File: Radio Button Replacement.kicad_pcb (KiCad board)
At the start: 2 copper layers, 40 x 40 mm, 19 parts, among them SW1 SW_Push_SPDT_1_3_2, SW2 SW_Push_SPDT_1_3_2, SW3 SW_Push_SPDT_1_3_2, SW4 SW_Push_SPDT_1_3_2

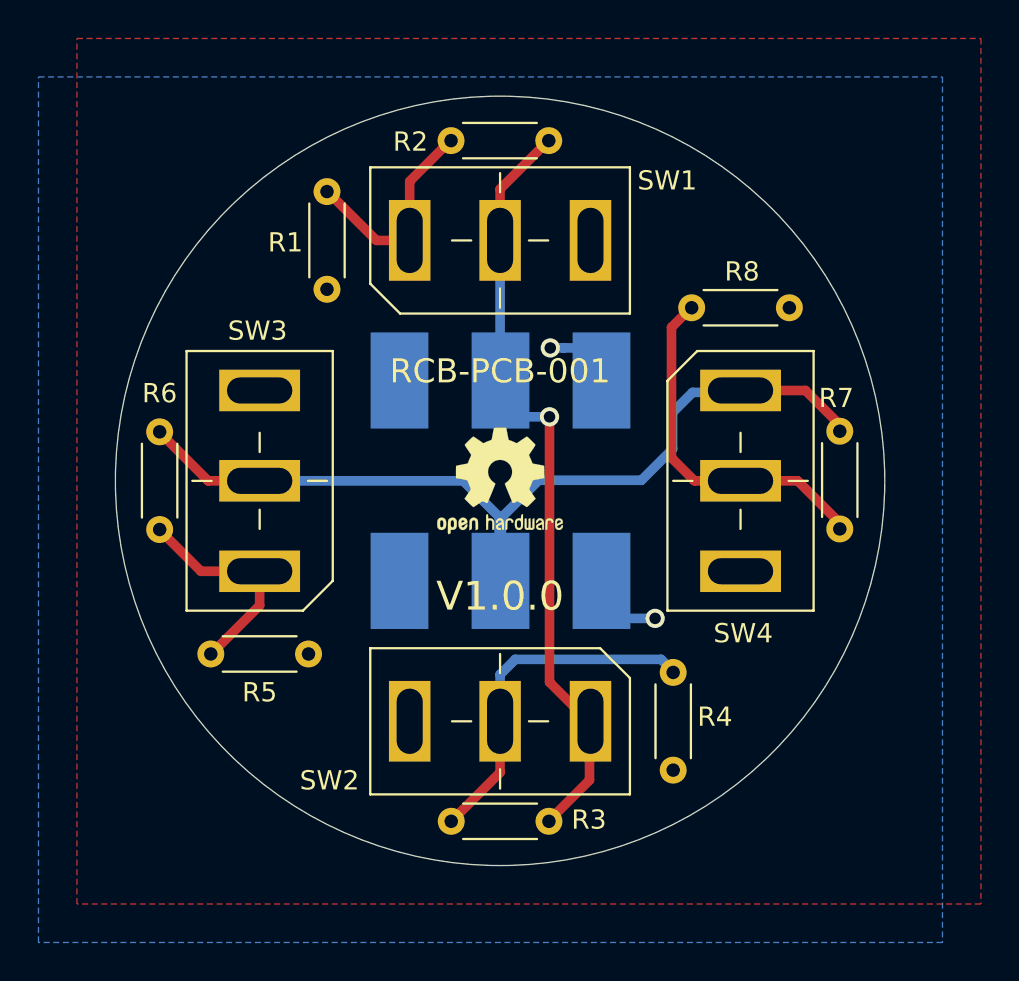
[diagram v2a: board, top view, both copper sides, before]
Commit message: Update resistor sizes
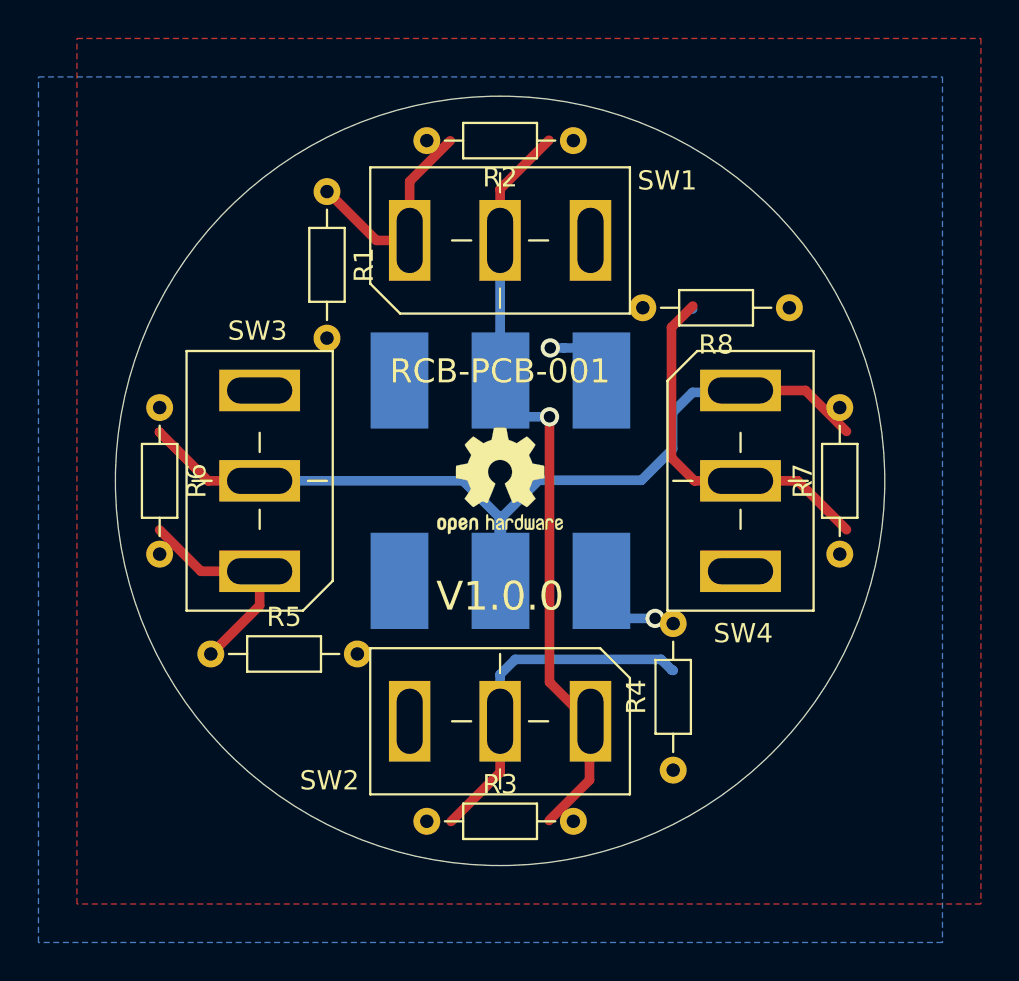
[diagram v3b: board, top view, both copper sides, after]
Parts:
- R1, R2, R3, R4, R5, R6, R7, R8: footprint Resistor_THT:R_Axial_DIN0204_L3.6mm_D1.6mm_P5.08mm_Horizontal -> Resistor_THT:R_Axial_DIN0204_L3.6mm_D1.6mm_P7.62mm_Horizontal
- moved R7 1.31 mm to (167.7, 103.8)
- moved R2 1.28 mm to (153.8, 82.3)
- moved R3 1.27 mm to (146.2, 117.7)
- moved R6 1.26 mm to (132.3, 96.2)

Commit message: Renumbering of components, PCB updates
Renumbering of components, PCB updates
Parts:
- removed the R8 at (165.0, 91.0)
- added R4: 2.2k, Resistor_THT:R_Axial_DIN0204_L3.6mm_D1.6mm_P7.62mm_Horizontal, F.Cu at (165.6, 91.0)
- moved SW1 17.7 mm to (137.5, 100.0), turned to 180 degrees
- moved SW3 17.7 mm to (150.0, 87.5), turned to 90 degrees
- moved R2 0.66 mm to (134.3, 109.0)
- moved R6 0.55 mm to (141.0, 84.4)
- moved R8 0.54 mm to (159.0, 115.6)
- renumbered R6 to R1, R5 to R2, R7 to R3, R2 to R5, R1 to R6, R3 to R7, R4 to R8, SW4 to SW2, SW2 to SW4
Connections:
- R1 pad 1: /WIRE2 -> /XWIRE
- R1 pad 2: Net-(R5-Pad1) -> Net-(R1-Pad2)
- R2 pad 1: Net-(R5-Pad1) -> Net-(R1-Pad2)
- R3 pad 2: /WIRE2 -> /XWIRE
- R5 pad 1: /WIRE1 -> /YWIRE
- R5 pad 2: Net-(R1-Pad1) -> Net-(R5-Pad2)
- R6 pad 1: Net-(R1-Pad1) -> Net-(R5-Pad2)
- R7 pad 2: /WIRE1 -> /YWIRE
- SW1 pad 1: Net-(R1-Pad1) -> Net-(R1-Pad2)
- SW1 pad 2: /WIRE1 -> /XWIRE
- SW2 pad 1: /WIRE2 -> /XWIRE
- SW3 pad 1: Net-(R5-Pad1) -> Net-(R5-Pad2)
- SW3 pad 2: /WIRE2 -> /YWIRE
- SW4 pad 1: /WIRE1 -> /YWIRE
- TP1 pad 2: /WIRE1 -> /XWIRE
- TP2 pad 2: /WIRE2 -> /YWIRE
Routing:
- net /WIRE2: track 50.2 -> 0.00 mm
- net /XWIRE: track 0.00 -> 47.9 mm
- net /YWIRE: track 0.00 -> 42.9 mm, vias 0 -> 2
- net /WIRE1: track 41.1 -> 0.00 mm, vias 1 -> 0
- net Net-(R1-Pad2): track 0.00 -> 12.1 mm
- net Net-(R5-Pad2): track 0.00 -> 11.9 mm
- net Net-(R1-Pad1): track 11.5 -> 0.00 mm
- net Net-(R5-Pad1): track 11.4 -> 0.00 mm
- net VBUS: track 7.94 -> 5.50 mm
- net Net-(R7-Pad1): track 18.3 -> 20.1 mm
- net Net-(R3-Pad1): track 19.1 -> 20.0 mm
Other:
- board text added: "X"
- board text added: "Y"
- board text removed: "1"
- board text removed: "2"

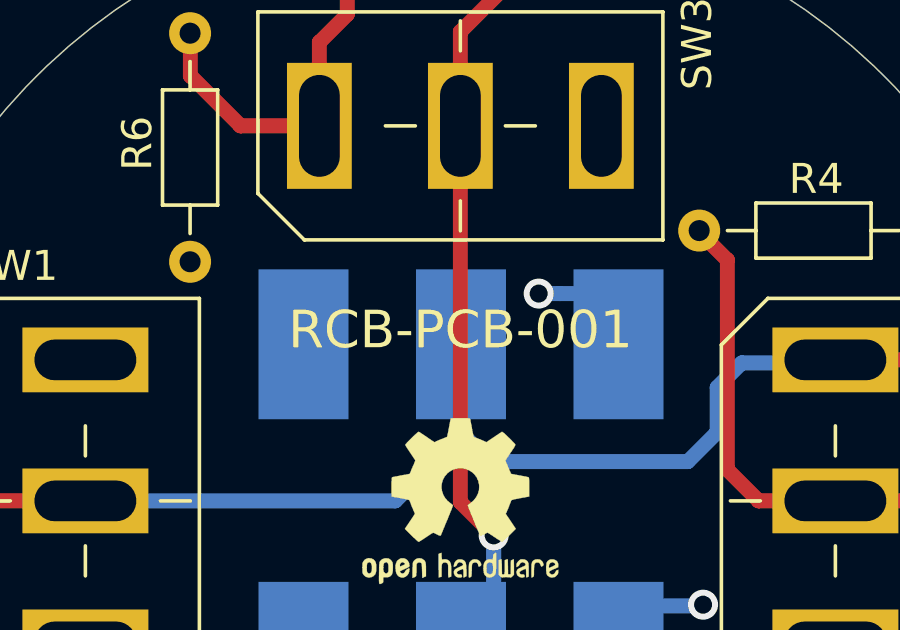
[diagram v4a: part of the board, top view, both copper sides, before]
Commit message: Update Radio Button Replacement.kicad_pcb
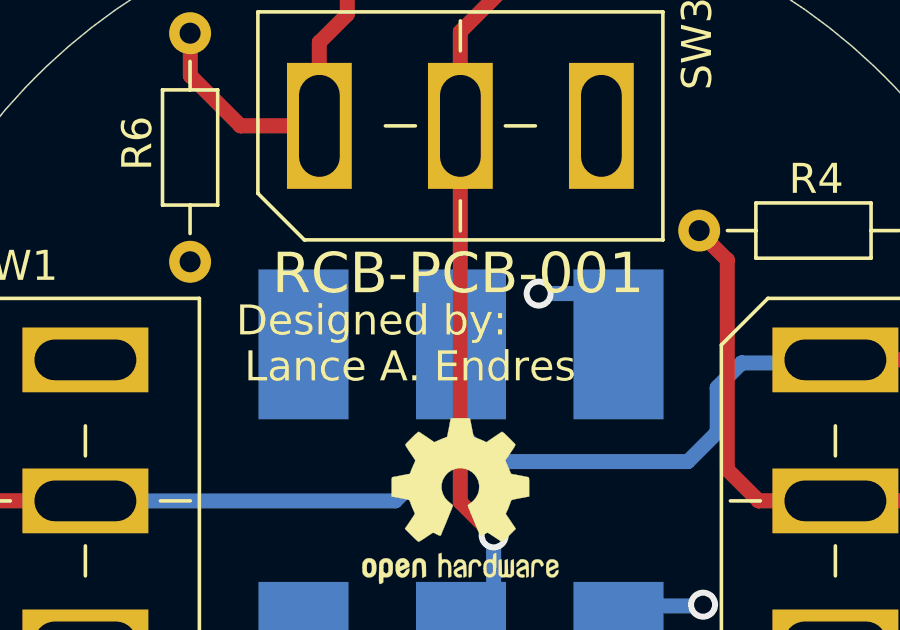
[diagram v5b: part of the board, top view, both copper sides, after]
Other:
- board text added: "Designed by:"
- board text added: "Lance A. Endres"
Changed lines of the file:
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@@
   (general
     (thickness 1.6)
-    (drawings 6)
+    (drawings 8)
     (tracks 74)
     (zones 0)
     (modules 19)
-    (nets 10)
+    (nets 9)
   )
   (page A4)
@@
   (net 5 /YWIRE)
   (net 6 /XWIRE)
-  (net 7 "Net-(SW4-Pad3)")
-  (net 8 "Net-(R1-Pad2)")
-  (net 9 "Net-(R5-Pad2)")
+  (net 7 "Net-(R1-Pad2)")
+  (net 8 "Net-(R5-Pad2)")
   (net_class Default "This is the default net class."
     (clearance 0.25)
@@
     (add_net "Net-(R5-Pad2)")
     (add_net "Net-(R7-Pad1)")
-    (add_net "Net-(SW1-Pad3)")
-    (add_net "Net-(SW2-Pad3)")
-    (add_net "Net-(SW3-Pad3)")
-    (add_net "Net-(SW4-Pad3)")
     (add_net VBUS)
   )
@@
       (net 6 /XWIRE))
     (pad 2 thru_hole oval (at 7.62 0 270) (size 1.4 1.4) (drill 0.7) (layers *.Cu *.Mask)
-      (net 8 "Net-(R1-Pad2)"))
+      (net 7 "Net-(R1-Pad2)"))
     (model ${KISYS3DMOD}/Resistor_THT.3dshapes/R_Axial_DIN0204_L3.6mm_D1.6mm_P7.62mm_Horizontal.wrl
       (at (xyz 0 0 0))
@@
       (net 1 VBUS))
     (pad 1 thru_hole circle (at 0 0) (size 1.4 1.4) (drill 0.7) (layers *.Cu *.Mask)
-      (net 8 "Net-(R1-Pad2)"))
+      (net 7 "Net-(R1-Pad2)"))
     (model ${KISYS3DMOD}/Resistor_THT.3dshapes/R_Axial_DIN0204_L3.6mm_D1.6mm_P7.62mm_Horizontal.wrl
       (at (xyz 0 0 0))
@@
       (net 5 /YWIRE))
     (pad 2 thru_hole oval (at 7.62 0 180) (size 1.4 1.4) (drill 0.7) (layers *.Cu *.Mask)
-      (net 9 "Net-(R5-Pad2)"))
+      (net 8 "Net-(R5-Pad2)"))
     (model ${KISYS3DMOD}/Resistor_THT.3dshapes/R_Axial_DIN0204_L3.6mm_D1.6mm_P7.62mm_Horizontal.wrl
       (at (xyz 0 0 0))
@@
       (net 1 VBUS))
     (pad 1 thru_hole circle (at 0 0 270) (size 1.4 1.4) (drill 0.7) (layers *.Cu *.Mask)
-      (net 9 "Net-(R5-Pad2)"))
+      (net 8 "Net-(R5-Pad2)"))
     (model ${KISYS3DMOD}/Resistor_THT.3dshapes/R_Axial_DIN0204_L3.6mm_D1.6mm_P7.62mm_Horizontal.wrl
       (at (xyz 0 0 0))
@@
       (net 5 /YWIRE))
     (pad 1 thru_hole rect (at 0 -4.7 90) (size 4.2 2.16) (drill oval 3.4 1.36) (layers *.Cu *.Mask)
-      (net 9 "Net-(R5-Pad2)"))
+      (net 8 "Net-(R5-Pad2)"))
     (model ${LE3DMOD}/8125SHZBE.step
       (offset (xyz 0 0 10))
@@
       (net 6 /XWIRE))
     (pad 1 thru_hole rect (at 0 -4.7 180) (size 4.2 2.16) (drill oval 3.4 1.36) (layers *.Cu *.Mask)
-      (net 8 "Net-(R1-Pad2)"))
+      (net 7 "Net-(R1-Pad2)"))
     (model ${LE3DMOD}/8125SHZBE.step
       (offset (xyz 0 0 10))
@@
       (net 3 GND) (solder_mask_margin 0.1016) (thermal_width 1.5))
   )
+  (gr_text "Lance A. Endres" (at 148.325238 95.52) (layer F.SilkS)
+    (effects (font (size 1 1) (thickness 0.15)))
+  )
+  (gr_text "Designed by:" (at 147.039524 93.98775) (layer F.SilkS)
+    (effects (font (size 1 1) (thickness 0.15)))
+  )
   (gr_circle (center 150 100) (end 168.05 100) (layer Dwgs.User) (width 0.05))
   (gr_text V1.0.0 (at 150 106) (layer F.SilkS)
     (effects (font (size 1.5 1.5) (thickness 0.3)))
   )
-  (gr_text RCB-PCB-001 (at 150 94.3) (layer F.SilkS)
-    (effects (font (size 1.25 1.25) (thickness 0.25)))
+  (gr_text RCB-PCB-001 (at 149.93 92.42) (layer F.SilkS)
+    (effects (font (size 1.35 1.35) (thickness 0.25)))
   )
   (gr_text Y (at 158.52 105.08) (layer B.SilkS)
@@
   )
   (gr_circle (center 150 100) (end 170 100) (layer Edge.Cuts) (width 0.05))
-  (segment (start 145.44 112.6) (end 145.46 112.58) (width 0.5) (layer B.Cu) (net 7))
   (via (at 152.61 93.09) (size 1) (drill 0.6) (layers F.Cu B.Cu) (net 1))
   (segment (start 153.317106 93.09) (end 152.61 93.09) (width 0.5) (layer B.Cu) (net 1))
@@
   (segment (start 155.34 105.24) (end 155.34 104.74) (width 0.5) (layer B.Cu) (net 1))
   (segment (start 155.34 104.74) (end 156.58 103.5) (width 0.5) (layer B.Cu) (net 1))
-  (segment (start 146.23 83.78) (end 146.23 82.32) (width 0.5) (layer F.Cu) (net 9))
-  (segment (start 145.3 87.5) (end 145.3 84.71) (width 0.5) (layer F.Cu) (net 9))
-  (segment (start 145.3 84.71) (end 146.23 83.78) (width 0.5) (layer F.Cu) (net 9))
+  (segment (start 158.9 98.96) (end 158.9 91.97) (width 0.5) (layer F.Cu) (net 2))
+  (segment (start 162.5 100) (end 159.94 100) (width 0.5) (layer F.Cu) (net 2))
+  (segment (start 158.9 91.97) (end 157.94 91.01) (width 0.5) (layer F.Cu) (net 2))
+  (segment (start 159.94 100) (end 158.9 98.96) (width 0.5) (layer F.Cu) (net 2))
+  (segment (start 162.5 100) (end 165.46 100) (width 0.5) (layer F.Cu) (net 2))
+  (segment (start 167.66 102.2) (end 167.66 103.79) (width 0.5) (layer F.Cu) (net 2))
+  (segment (start 165.46 100) (end 167.66 102.2) (width 0.5) (layer F.Cu) (net 2))
+  (segment (start 157.96 109.03) (end 158.99 108) (width 0.5) (layer B.Cu) (net 4))
+  (segment (start 151.04 109.03) (end 157.96 109.03) (width 0.5) (layer B.Cu) (net 4))
+  (segment (start 150 112.5) (end 150 110.07) (width 0.5) (layer B.Cu) (net 4))
+  (segment (start 150 110.07) (end 151.04 109.03) (width 0.5) (layer B.Cu) (net 4))
+  (segment (start 150 115.55) (end 150 112.42) (width 0.5) (layer F.Cu) (net 4))
+  (segment (start 146.2 117.65) (end 147.9 117.65) (width 0.5) (layer F.Cu) (net 4))
+  (segment (start 147.9 117.65) (end 150 115.55) (width 0.5) (layer F.Cu) (net 4))
   (segment (start 150 87.51) (end 150.06 87.45) (width 0.5) (layer B.Cu) (net 5))
   (segment (start 150.04 87.4) (end 150.19 87.55) (width 0.5) (layer B.Cu) (net 5))
@@
   (segment (start 152.06 82.3) (end 153.8 82.3) (width 0.5) (layer F.Cu) (net 5))
   (segment (start 150 84.36) (end 152.06 82.3) (width 0.5) (layer F.Cu) (net 5))
-  (segment (start 157.96 109.03) (end 158.99 108) (width 0.5) (layer B.Cu) (net 4))
-  (segment (start 151.04 109.03) (end 157.96 109.03) (width 0.5) (layer B.Cu) (net 4))
-  (segment (start 150 112.5) (end 150 110.07) (width 0.5) (layer B.Cu) (net 4))
-  (segment (start 150 110.07) (end 151.04 109.03) (width 0.5) (layer B.Cu) (net 4))
-  (segment (start 133.59 103.84) (end 132.35 103.84) (width 0.5) (layer F.Cu) (net 8))
-  (segment (start 137.5 104.7) (end 134.45 104.7) (width 0.5) (layer F.Cu) (net 8))
-  (segment (start 134.45 104.7) (end 133.59 103.84) (width 0.5) (layer F.Cu) (net 8))
-  (segment (start 135.97 109.05) (end 134.35 109.05) (width 0.5) (layer F.Cu) (net 8))
-  (segment (start 137.5 104.7) (end 137.5 107.52) (width 0.5) (layer F.Cu) (net 8))
-  (segment (start 137.5 107.52) (end 135.97 109.05) (width 0.5) (layer F.Cu) (net 8))
-  (segment (start 166.33 96.23) (end 167.64 96.23) (width 0.5) (layer F.Cu) (net 6))
-  (segment (start 162.5 95.3) (end 165.4 95.3) (width 0.5) (layer F.Cu) (net 6))
-  (segment (start 165.4 95.3) (end 166.33 96.23) (width 0.5) (layer F.Cu) (net 6))
-  (segment (start 158.9 98.96) (end 158.9 91.97) (width 0.5) (layer F.Cu) (net 2))
-  (segment (start 162.5 100) (end 159.94 100) (width 0.5) (layer F.Cu) (net 2))
-  (segment (start 158.9 91.97) (end 157.94 91.01) (width 0.5) (layer F.Cu) (net 2))
-  (segment (start 159.94 100) (end 158.9 98.96) (width 0.5) (layer F.Cu) (net 2))
-  (segment (start 162.5 100) (end 165.46 100) (width 0.5) (layer F.Cu) (net 2))
-  (segment (start 167.66 102.2) (end 167.66 103.79) (width 0.5) (layer F.Cu) (net 2))
-  (segment (start 165.46 100) (end 167.66 102.2) (width 0.5) (layer F.Cu) (net 2))
-  (segment (start 145.3 87.5) (end 142.67 87.5) (width 0.5) (layer F.Cu) (net 9))
-  (segment (start 141 85.83) (end 141 84.46) (width 0.5) (layer F.Cu) (net 9))
-  (segment (start 142.67 87.5) (end 141 85.83) (width 0.5) (layer F.Cu) (net 9))
-  (segment (start 150 115.55) (end 150 112.42) (width 0.5) (layer F.Cu) (net 4))
-  (segment (start 146.2 117.65) (end 147.9 117.65) (width 0.5) (layer F.Cu) (net 4))
-  (segment (start 147.9 117.65) (end 150 115.55) (width 0.5) (layer F.Cu) (net 4))
   (via (at 152.53 107.319998) (size 1) (drill 0.6) (layers F.Cu B.Cu) (net 5))
   (segment (start 150.619998 107.319998) (end 151.822894 107.319998) (width 0.5) (layer B.Cu) (net 5))
@@
   (segment (start 150.02 105.2) (end 150.07 105.2) (width 0.5) (layer B.Cu) (net 5))
   (segment (start 150.07 105.2) (end 151.110002 104.159998) (width 0.5) (layer B.Cu) (net 5))
+  (segment (start 166.33 96.23) (end 167.64 96.23) (width 0.5) (layer F.Cu) (net 6))
+  (segment (start 162.5 95.3) (end 165.4 95.3) (width 0.5) (layer F.Cu) (net 6))
+  (segment (start 165.4 95.3) (end 166.33 96.23) (width 0.5) (layer F.Cu) (net 6))
   (segment (start 132.34 97.84) (end 132.34 96.25) (width 0.5) (layer F.Cu) (net 6))
   (segment (start 137.5 100) (end 134.5 100) (width 0.5) (layer F.Cu) (net 6))
@@
   (segment (start 150.98 98.69) (end 157.58 98.69) (width 0.5) (layer B.Cu) (net 6))
   (segment (start 157.58 98.69) (end 158.56 97.71) (width 0.5) (layer B.Cu) (net 6))
+  (segment (start 145.44 112.6) (end 145.46 112.58) (width 0.5) (layer B.Cu) (net 0))
+  (segment (start 133.59 103.84) (end 132.35 103.84) (width 0.5) (layer F.Cu) (net 7))
+  (segment (start 137.5 104.7) (end 134.45 104.7) (width 0.5) (layer F.Cu) (net 7))
+  (segment (start 134.45 104.7) (end 133.59 103.84) (width 0.5) (layer F.Cu) (net 7))
+  (segment (start 135.97 109.05) (end 134.35 109.05) (width 0.5) (layer F.Cu) (net 7))
+  (segment (start 137.5 104.7) (end 137.5 107.52) (width 0.5) (layer F.Cu) (net 7))
+  (segment (start 137.5 107.52) (end 135.97 109.05) (width 0.5) (layer F.Cu) (net 7))
+  (segment (start 146.23 83.78) (end 146.23 82.32) (width 0.5) (layer F.Cu) (net 8))
+  (segment (start 145.3 87.5) (end 145.3 84.71) (width 0.5) (layer F.Cu) (net 8))
+  (segment (start 145.3 84.71) (end 146.23 83.78) (width 0.5) (layer F.Cu) (net 8))
+  (segment (start 145.3 87.5) (end 142.67 87.5) (width 0.5) (layer F.Cu) (net 8))
+  (segment (start 141 85.83) (end 141 84.46) (width 0.5) (layer F.Cu) (net 8))
+  (segment (start 142.67 87.5) (end 141 85.83) (width 0.5) (layer F.Cu) (net 8))
   (zone (net 1) (net_name VBUS) (layer F.Cu) (hatch edge 0.508)
     (connect_pads (clearance 0.25))
